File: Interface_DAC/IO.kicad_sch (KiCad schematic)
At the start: 8 parts, among them J1 USB_C_Receptacle_USB2.0_16P, J2 Conn_Coaxial, U6 SN74LVC2G14DBV, U7 FUSB302BMPX

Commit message: Footprint Arrangement
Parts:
- C36, C42: footprint (none) -> Capacitor_SMD:C_0402_1005Metric
- J1: footprint (none) -> Connector_USB:USB_C_Receptacle_GCT_USB4110
- J2: footprint (none) -> utils:PJRAN1X1U04
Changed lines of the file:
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@@
 			)
 		)
-		(property "Footprint" ""
+		(property "Footprint" "utils:PJRAN1X1U04"
 			(at 118.11 115.57 0)
 			(effects
@@
 			)
 		)
-		(property "Footprint" ""
+		(property "Footprint" "Connector_USB:USB_C_Receptacle_GCT_USB4110"
 			(at 50.8 128.27 0)
 			(effects
@@
 			)
 		)
-		(property "Footprint" ""
+		(property "Footprint" "Capacitor_SMD:C_0402_1005Metric"
 			(at 42.8752 50.8 0)
 			(effects
@@
 			)
 		)
-		(property "Footprint" ""
+		(property "Footprint" "Capacitor_SMD:C_0402_1005Metric"
 			(at 32.7152 50.8 0)
 			(effects

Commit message: Schematic Tinkering and PCB Layout
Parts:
- removed C36: 1u, Capacitor_SMD:C_0402_1005Metric, symbol Device:C
- removed U7: FUSB302BMPX, Package_DFN_QFN:WQFN-14-1EP_2.5x2.5mm_P0.5mm_EP1.45x1.45mm, symbol Interface_USB:FUSB302BMPX
- added J1: Barrel_Jack_Switch_Pin3Ring, utils:DC044, symbol Connector:Barrel_Jack_Switch_Pin3Ring
- added L2: 0805USB, Inductor_SMD:L_CommonModeChoke_Coilcraft_0805USB, symbol Device:L_Coupled_1243
- added R8: 47k, Resistor_SMD:R_0402_1005Metric, symbol Device:R
- added U5: TUSB320, Package_DFN_QFN:Texas_X2QFN-12_1.6x1.6mm_P0.4mm, symbol Interface_USB:TUSB320
- renumbered C42 to C49, D1 to D2, J1 to J3
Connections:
- net +3.3V: now also U5.12 (VDD)
- net CC1: now also U5.1 (CC1)
- net CC2: now also U5.2 (CC2)
- net FUSB302_INT_N: now also U5.6 (~{INT}/OUT3)
- net GND: now also R8.2, U5.10 (GND), U5.11 (~{EN}), U5.5 (ADDR)
- net I2C_SCL: now also U5.8 (SCL/OUT2)
- net I2C_SDA: now also U5.7 (SDA/OUT1)
- net USB_DN: now also L2.1; no longer D2.3 (I/O2), J3.A7 (D-), J3.B7 (D-)
- net USB_DP: now also L2.4; no longer D2.2 (I/O1), J3.A6 (D+), J3.B6 (D+)
- net VBUS: now also U5.4 (VBUS_DET)
- new net: R8.1, U5.3 (PORT)
- new net PRE_USB_DN: D2.2 (I/O1), J3.A7 (D-), J3.B7 (D-), L2.2
- new net PRE_USB_DP: D2.3 (I/O2), J3.A6 (D+), J3.B6 (D+), L2.3
- no-connect marks 2 -> 0
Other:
- moved on the sheet: C49

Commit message: Schematic Tinkering and PCB Layout
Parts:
- renumbered C49 to C57, R8 to R21, U5 to U8, U6 to U9
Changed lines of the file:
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@@
 		(dnp no)
 		(fields_autoplaced yes)
-		(property "Reference" "#PWR066"
+		(property "Reference" "#PWR076"
 			(at 36.83 78.74 0)
 			(effects
@@
 			(project "Interface_DAC"
 				(path "/0e211ec1-40f7-401e-8406-03ff71d7b636/5d69970a-4a66-4f83-8db7-c703f3245971"
-					(reference "#PWR066")
+					(reference "#PWR076")
 					(unit 1)
 				)
@@
 		(dnp no)
 		(fields_autoplaced yes)
-		(property "Reference" "U5"
+		(property "Reference" "U8"
 			(at 56.7533 49.53 0)
 			(effects
@@
 			(project ""
 				(path "/0e211ec1-40f7-401e-8406-03ff71d7b636/5d69970a-4a66-4f83-8db7-c703f3245971"
-					(reference "U5")
+					(reference "U8")
 					(unit 1)
 				)
@@
 		(dnp no)
 		(fields_autoplaced yes)
-		(property "Reference" "#PWR072"
+		(property "Reference" "#PWR082"
 			(at 46.99 160.02 0)
 			(effects
@@
 			(project "Interface_DAC"
 				(path "/0e211ec1-40f7-401e-8406-03ff71d7b636/5d69970a-4a66-4f83-8db7-c703f3245971"
-					(reference "#PWR072")
+					(reference "#PWR082")
 					(unit 1)
 				)
@@
 		(dnp no)
 		(fields_autoplaced yes)
-		(property "Reference" "#PWR064"
+		(property "Reference" "#PWR074"
 			(at 72.39 58.42 0)
 			(effects
@@
 			(project "Interface_DAC"
 				(path "/0e211ec1-40f7-401e-8406-03ff71d7b636/5d69970a-4a66-4f83-8db7-c703f3245971"
-					(reference "#PWR064")
+					(reference "#PWR074")
 					(unit 1)
 				)
@@
 		(dnp no)
 		(fields_autoplaced yes)
-		(property "Reference" "R8"
+		(property "Reference" "R21"
 			(at 82.55 74.9299 0)
 			(effects
@@
 			(project ""
 				(path "/0e211ec1-40f7-401e-8406-03ff71d7b636/5d69970a-4a66-4f83-8db7-c703f3245971"
-					(reference "R8")
+					(reference "R21")
 					(unit 1)
 				)
@@
 		(dnp no)
 		(fields_autoplaced yes)
-		(property "Reference" "#PWR065"
+		(property "Reference" "#PWR075"
 			(at 144.78 58.42 0)
 			(effects
@@
 			(project "Interface_DAC"
 				(path "/0e211ec1-40f7-401e-8406-03ff71d7b636/5d69970a-4a66-4f83-8db7-c703f3245971"
-					(reference "#PWR065")
+					(reference "#PWR075")
 					(unit 1)
 				)
@@
 		(dnp no)
 		(fields_autoplaced yes)
-		(property "Reference" "U6"
+		(property "Reference" "U9"
 			(at 172.3233 107.95 0)
 			(effects
@@
 			(project ""
 				(path "/0e211ec1-40f7-401e-8406-03ff71d7b636/5d69970a-4a66-4f83-8db7-c703f3245971"
-					(reference "U6")
+					(reference "U9")
 					(unit 1)
 				)
@@
 		(dnp no)
 		(fields_autoplaced yes)
-		(property "Reference" "#PWR071"
+		(property "Reference" "#PWR081"
 			(at 64.77 114.3 0)
 			(effects
@@
 			(project "Interface_DAC"
 				(path "/0e211ec1-40f7-401e-8406-03ff71d7b636/5d69970a-4a66-4f83-8db7-c703f3245971"
-					(reference "#PWR071")
+					(reference "#PWR081")
 					(unit 1)
 				)
@@
 		(dnp no)
 		(fields_autoplaced yes)
-		(property "Reference" "#PWR063"
+		(property "Reference" "#PWR073"
 			(at 44.45 53.34 0)
 			(effects
@@
 			(project "Interface_DAC"
 				(path "/0e211ec1-40f7-401e-8406-03ff71d7b636/5d69970a-4a66-4f83-8db7-c703f3245971"
-					(reference "#PWR063")
+					(reference "#PWR073")
 					(unit 1)
 				)
@@
 		(dnp no)
 		(fields_autoplaced yes)
-		(property "Reference" "#PWR062"
+		(property "Reference" "#PWR072"
 			(at 44.45 35.56 0)
 			(effects
@@
 			(project "Interface_DAC"
 				(path "/0e211ec1-40f7-401e-8406-03ff71d7b636/5d69970a-4a66-4f83-8db7-c703f3245971"
-					(reference "#PWR062")
+					(reference "#PWR072")
 					(unit 1)
 				)
@@
 		(on_board yes)
 		(dnp no)
-		(property "Reference" "C49"
+		(property "Reference" "C57"
 			(at 46.99 39.37 0)
 			(effects
@@
 			(project "Interface_DAC"
 				(path "/0e211ec1-40f7-401e-8406-03ff71d7b636/5d69970a-4a66-4f83-8db7-c703f3245971"
-					(reference "C49")
+					(reference "C57")
 					(unit 1)
 				)
@@
 		(dnp no)
 		(fields_autoplaced yes)
-		(property "Reference" "#PWR070"
+		(property "Reference" "#PWR080"
 			(at 144.78 91.44 0)
 			(effects
@@
 			(project "Interface_DAC"
 				(path "/0e211ec1-40f7-401e-8406-03ff71d7b636/5d69970a-4a66-4f83-8db7-c703f3245971"
-					(reference "#PWR070")
+					(reference "#PWR080")
 					(unit 1)
 				)
@@
 		(dnp no)
 		(fields_autoplaced yes)
-		(property "Reference" "#PWR069"
+		(property "Reference" "#PWR079"
 			(at 80.01 88.9 0)
 			(effects
@@
 			(project "Interface_DAC"
 				(path "/0e211ec1-40f7-401e-8406-03ff71d7b636/5d69970a-4a66-4f83-8db7-c703f3245971"
-					(reference "#PWR069")
+					(reference "#PWR079")
 					(unit 1)
 				)
@@
 		(dnp no)
 		(fields_autoplaced yes)
-		(property "Reference" "#PWR068"
+		(property "Reference" "#PWR078"
 			(at 54.61 86.36 0)
 			(effects
@@
 			(project "Interface_DAC"
 				(path "/0e211ec1-40f7-401e-8406-03ff71d7b636/5d69970a-4a66-4f83-8db7-c703f3245971"
-					(reference "#PWR068")
+					(reference "#PWR078")
 					(unit 1)
 				)
@@
 		(dnp no)
 		(fields_autoplaced yes)
-		(property "Reference" "#PWR067"
+		(property "Reference" "#PWR077"
 			(at 72.39 81.28 0)
 			(effects
@@
 			(project "Interface_DAC"
 				(path "/0e211ec1-40f7-401e-8406-03ff71d7b636/5d69970a-4a66-4f83-8db7-c703f3245971"
-					(reference "#PWR067")
-					(unit 1)
-				)
+					(reference "#PWR077")
+					(unit 1)
+				)

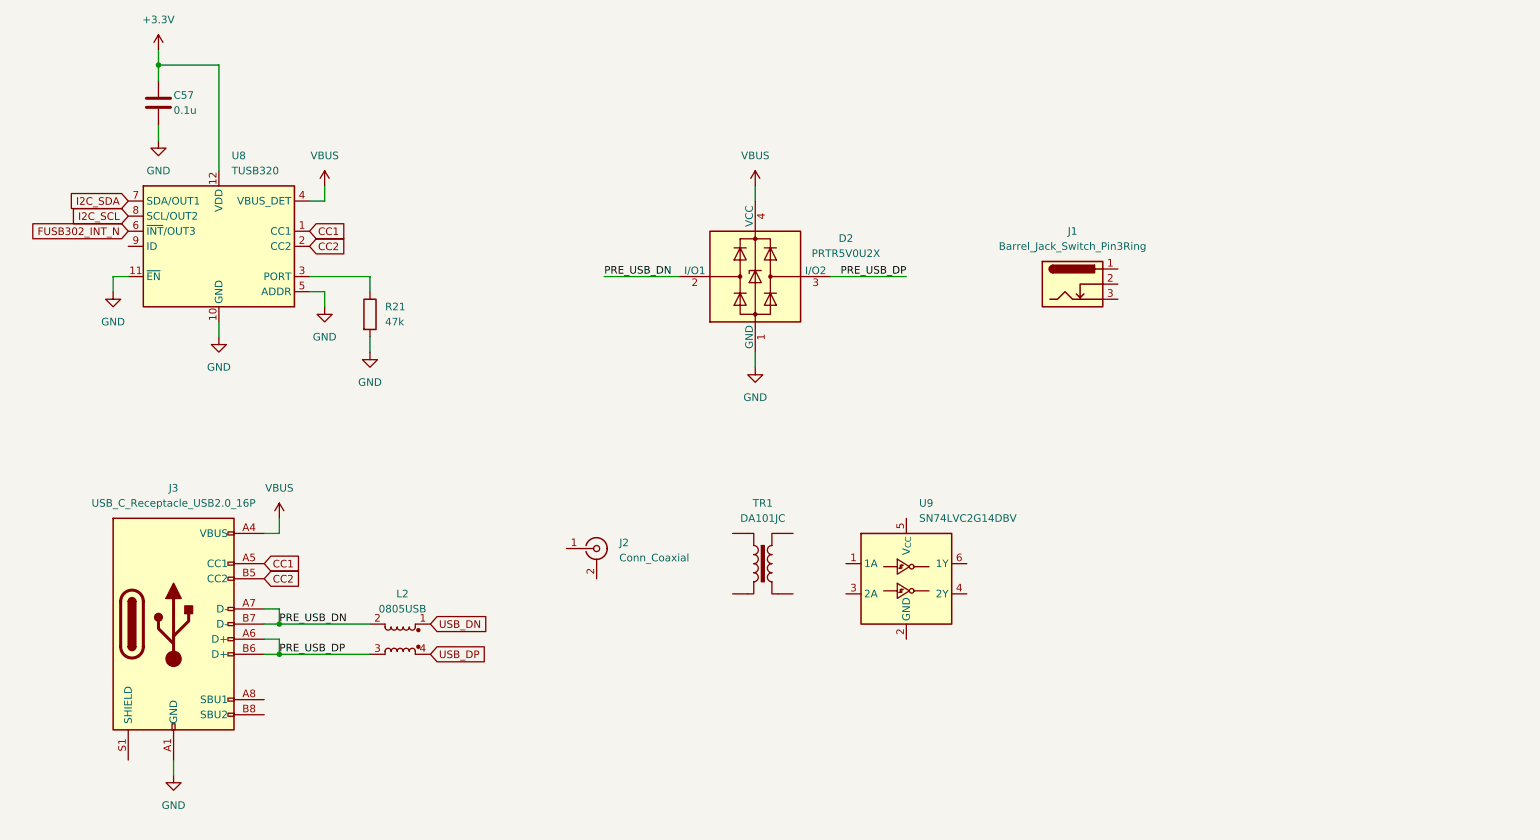
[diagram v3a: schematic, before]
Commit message: Schematic Design and Library Relink
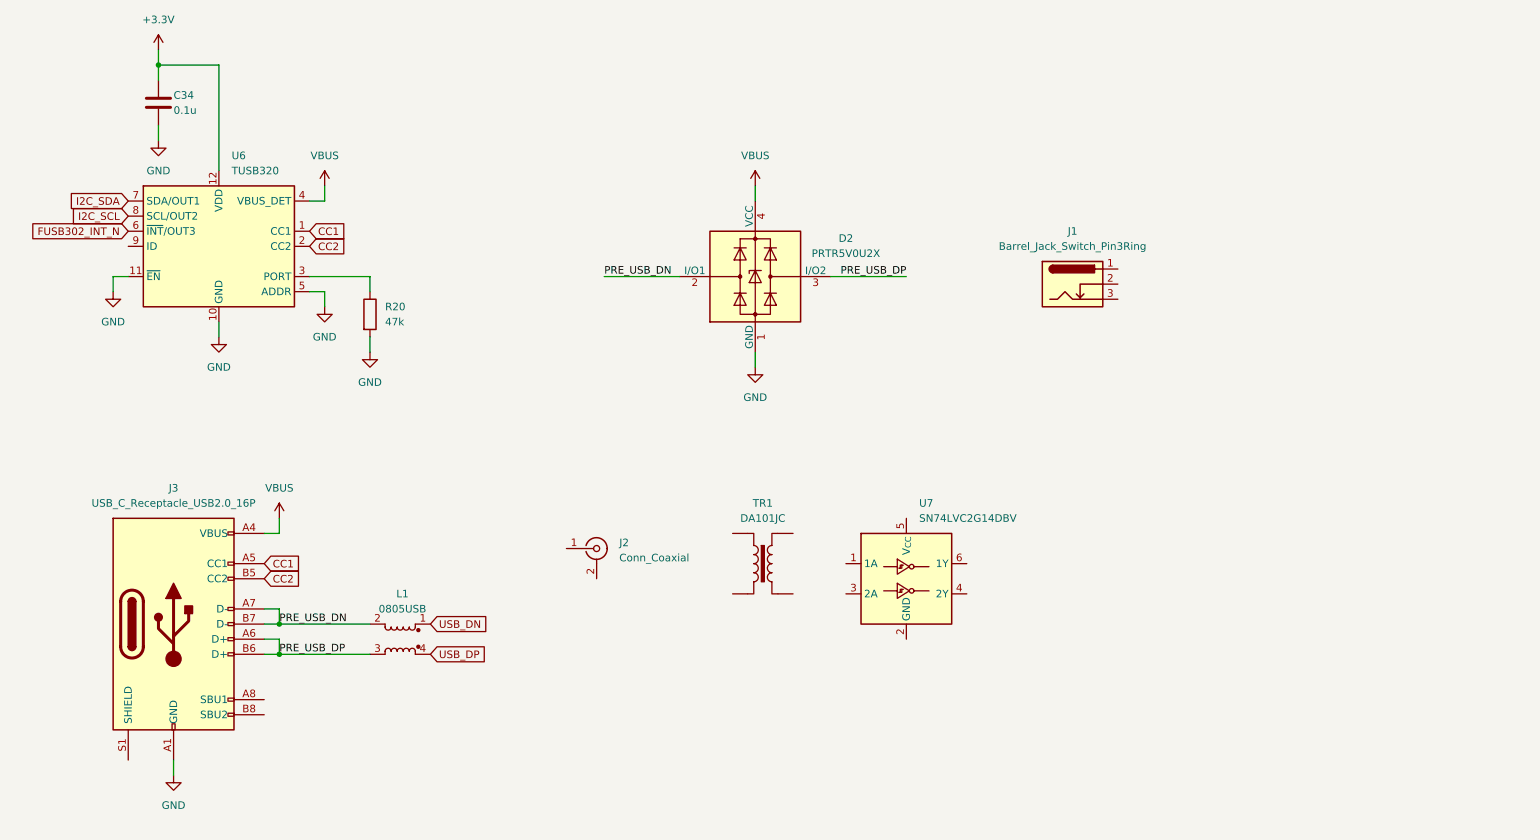
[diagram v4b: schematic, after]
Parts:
- renumbered C57 to C34, L2 to L1, R21 to R20, U8 to U6, U9 to U7

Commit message: Schematic Design
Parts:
- added C35: 0.1u, Capacitor_SMD:C_0402_1005Metric, symbol Device:C
- added C36, C37, C38: 4.7u, Capacitor_SMD:C_0402_1005Metric, symbol Device:C
- added C39, C40: 8p, Capacitor_SMD:C_0402_1005Metric, symbol Device:C
- added R21: 10k, Resistor_SMD:R_0402_1005Metric, symbol Device:R
- added R23: 1M, Resistor_SMD:R_0402_1005Metric, symbol Device:R
- added R24: 12k, Resistor_SMD:R_0402_1005Metric, symbol Device:R
- added U7: USB3300-EZK, Package_DFN_QFN:QFN-32-1EP_5x5mm_P0.5mm_EP3.45x3.45mm, symbol Interface_USB:USB3300-EZK
- added Y4: 24M, Crystal:Crystal_SMD_2016-4Pin_2.0x1.6mm, symbol Device:Crystal_GND24
- renumbered J3 to J2, J2 to J3, R20 to R22, U7 to U8
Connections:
- net GND: now also C35.2, C36.2, C37.2, C38.2, C39.2, C40.2, R24.2, U7.1 (GND), U7.2 (GND), U7.33 (GND), Y4.2, Y4.4
- net USB_DN: now also U7.8 (DM)
- net USB_DP: now also U7.7 (DP)
- net VBUS: now also C37.1, R21.1
- new net: C39.1, R23.2, U7.27 (XO), Y4.3
- new net: C36.1, U7.15 (VDD1.8), U7.26 (VDD1.8)
- new net: R21.2, U7.4 (VBUS)
- new net: C40.1, R23.1, U7.28 (XI), Y4.1
- new net: R24.1, U7.32 (RBIAS)
- new net: C38.1, U7.29 (VDDA1.8)
- new net REG_EN: C35.1, U7.16 (VDD3.3), U7.25 (VDD3.3), U7.30 (VDD3.3), U7.31 (REG_EN), U7.6 (VDD3.3)
- new net ULPI_CK: U7.14 (CLKOUT)
- new net ULPI_D0: U7.24 (DATA0)
- new net ULPI_D1: U7.23 (DATA1)
- new net ULPI_D2: U7.22 (DATA2)
- new net ULPI_D3: U7.21 (DATA3)
- new net ULPI_D4: U7.20 (DATA4)
- new net ULPI_D5: U7.19 (DATA5)
- new net ULPI_D6: U7.18 (DATA6)
- new net ULPI_D7: U7.17 (DATA7)
- new net ULPI_DIR: U7.12 (DIR)
- new net ULPI_NXT: U7.11 (NXT)
- new net ULPI_STP: U7.13 (STP)
- no-connect marks 0 -> 3
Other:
- moved on the sheet: D2, J1, J3, TR1, U8

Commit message: Update IO.kicad_sch
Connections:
- net REG_EN is gone; now on net +3.3V: C35.1, U7.16 (VDD3.3), U7.25 (VDD3.3), U7.30 (VDD3.3), U7.31 (REG_EN), U7.6 (VDD3.3)
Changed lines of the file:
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@@
+	)
+	(junction
+		(at 237.49 34.29)
+		(diameter 0)
+		(color 0 0 0 0)
 	)
 	(junction
@@
 		(pts
 			(xy 64.77 128.27) (xy 62.23 128.27)
+		)
+		(stroke
+			(width 0)
+			(type default)
+		)
+	)
+	(wire
+		(pts
+			(xy 237.49 31.75) (xy 237.49 34.29)
 		)
 		(stroke
@@
 					(unit 1)
 				)
+			)
+		)
+	)
+	(symbol
+		(lib_id "power:+3.3V")
+		(at 237.49 31.75 0)
+		(unit 1)
+		(exclude_from_sim no)
+		(in_bom yes)
+		(on_board yes)
+		(dnp no)
+		(fields_autoplaced yes)
+		(property "Reference" "#PWR098"
+			(at 237.49 35.56 0)
+			(effects
+				(font
+					(size 1.27 1.27)
+				)
+				(hide yes)
+			)
+		)
+		(property "Value" "+3.3V"
+			(at 237.49 26.67 0)
+			(effects
+				(font
+					(size 1.27 1.27)
+				)
+			)
+		)
+		(property "Footprint" ""
+			(at 237.49 31.75 0)
+			(effects
+				(font
+					(size 1.27 1.27)
+				)
+				(hide yes)
+			)
+		)
+		(property "Datasheet" ""
+			(at 237.49 31.75 0)
+			(effects
+				(font
+					(size 1.27 1.27)
+				)
+				(hide yes)
+			)
+		)
+		(property "Description" "Power symbol creates a global label with name \"+3.3V\""
+			(at 237.49 31.75 0)
+			(effects
+				(font
+					(size 1.27 1.27)
+				)
+				(hide yes)
+			)
+		)
+		(pin "1"
+		)
+		(instances
+			(project "Interface_DAC"
+				(path "/0e211ec1-40f7-401e-8406-03ff71d7b636/5d69970a-4a66-4f83-8db7-c703f3245971"
+					(reference "#PWR098")
+					(unit 1)
+				)
